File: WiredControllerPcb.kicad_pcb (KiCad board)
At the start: 2 copper layers, 90 x 50 mm, 40 parts, among them J1 Joystick, J2 Conn_01x06, J3 Conn_01x04, J4 Conn_01x04, J5 Conn_01x04, SW1 SW_Push, SW2 SW_Push, SW3 SW_Push, SW4 SW_Push, U1 LP2985-3.3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

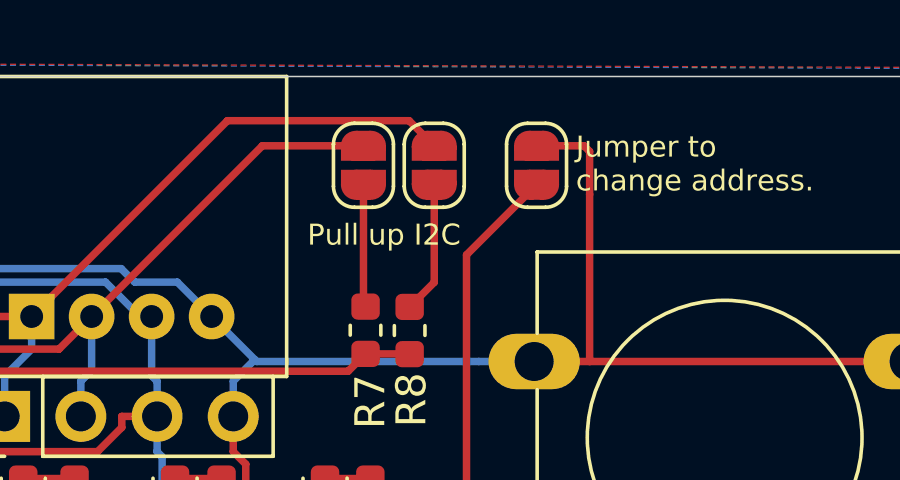
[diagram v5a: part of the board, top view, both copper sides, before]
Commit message: Update for KiCad6
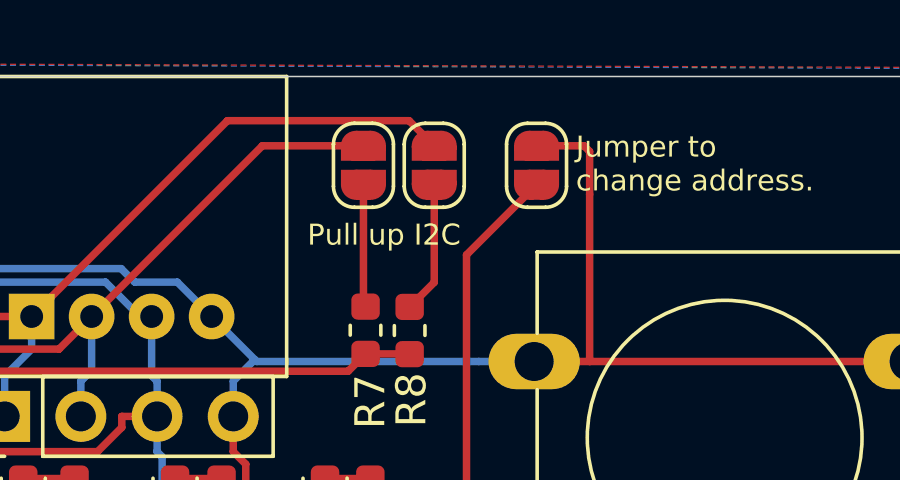
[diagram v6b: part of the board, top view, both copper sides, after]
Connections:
- U2 pad 1: Net-(U2-Pad1) -> unconnected-(U2-Pad1)
- U2 pad 19: Net-(U2-Pad19) -> unconnected-(U2-Pad19)
- U2 pad 22: Net-(U2-Pad22) -> unconnected-(U2-Pad22)
- U2 pad 7: Net-(U2-Pad7) -> unconnected-(U2-Pad7)
- U2 pad 8: Net-(U2-Pad8) -> unconnected-(U2-Pad8)
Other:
- net class Default removed
